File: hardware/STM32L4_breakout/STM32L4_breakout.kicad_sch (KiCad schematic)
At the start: 66 parts, among them J1 12V IN, J10 GPIO, J12 USART1, J13 USART3, J15 3.3V, J16 5V, J17 12V, J2 SWD, J3 Conn_01x08, J4 Conn_01x06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

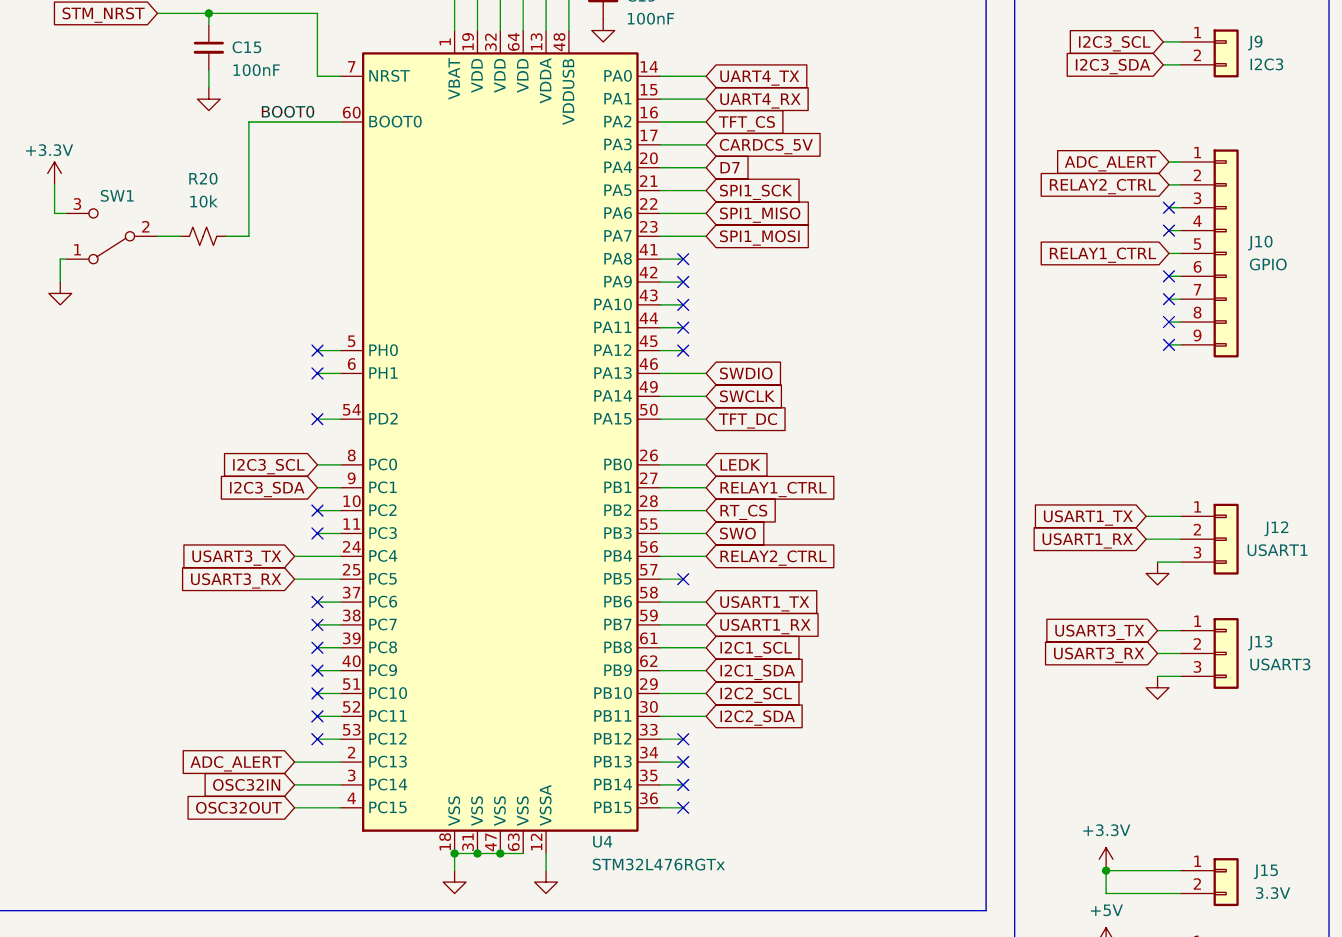
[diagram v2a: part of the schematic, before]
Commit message: moved GPIO signals on schematic
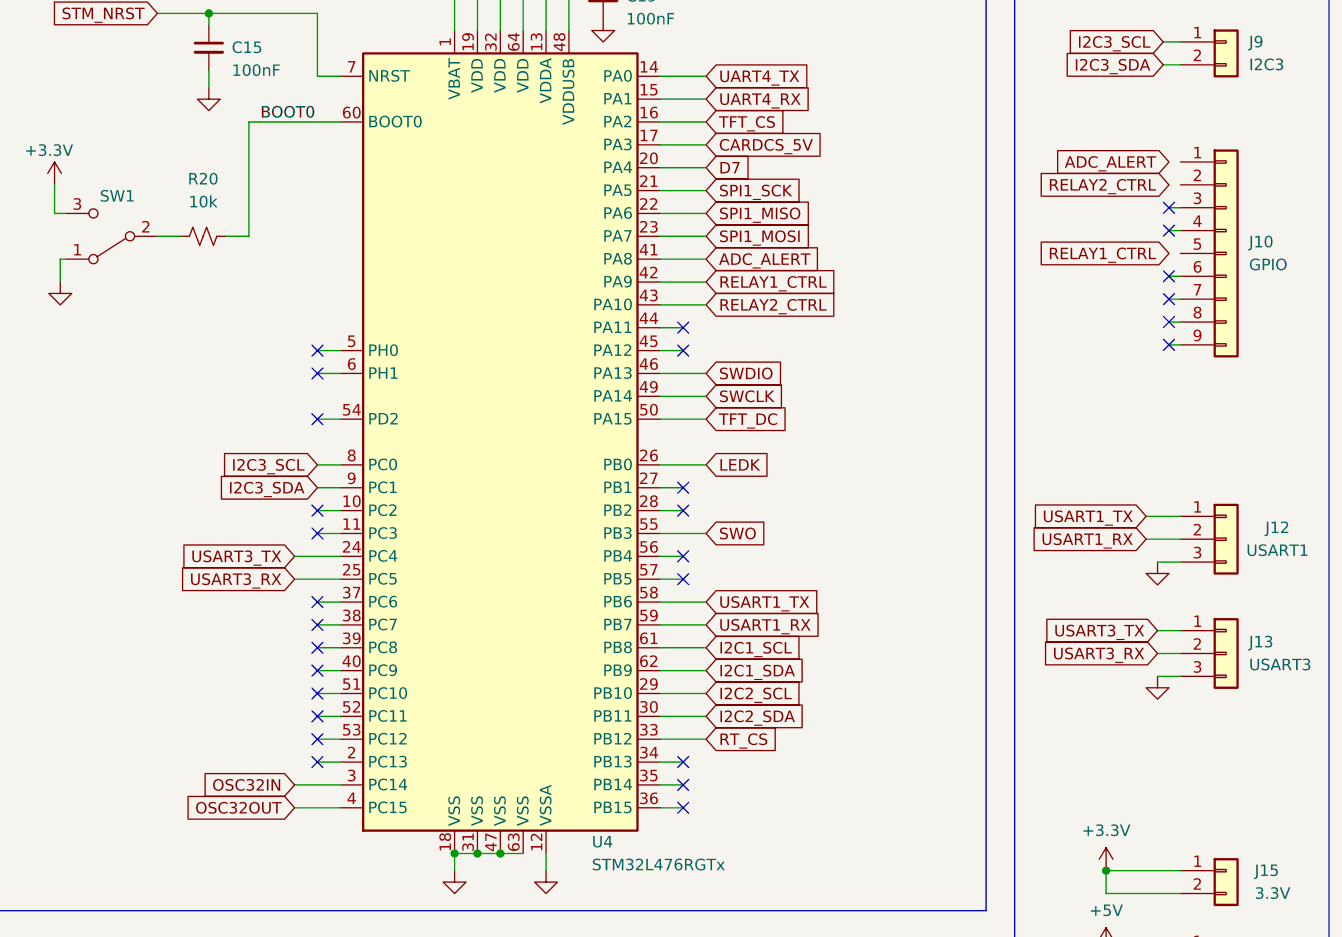
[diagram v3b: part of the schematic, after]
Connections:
- net ADC_ALERT: now also U4.41 (PA8); no longer J10.1 (Pin_1), U4.2 (PC13)
- net RELAY1_CTRL: now also U4.42 (PA9); no longer J10.5 (Pin_5), U4.27 (PB1)
- net RELAY2_CTRL: now also U4.43 (PA10); no longer J10.2 (Pin_2), U4.56 (PB4)
- net RT_CS: now also U4.33 (PB12); no longer U4.28 (PB2)
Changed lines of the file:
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@@
   (junction (at 159.385 36.83) (diameter 0) (color 0 0 0 0)
   )
-  (no_connect (at 209.55 125.73))
+  (no_connect (at 209.55 97.79))
   (no_connect (at 24.13 183.515))
   (no_connect (at 168.91 82.55))
@@
   (no_connect (at 24.13 178.435))
   (no_connect (at 62.865 180.975))
-  (no_connect (at 209.55 72.39))
   (no_connect (at 168.91 100.33))
-  (no_connect (at 209.55 77.47))
   (no_connect (at 168.91 120.65))
-  (no_connect (at 209.55 74.93))
   (no_connect (at 263.525 81.915))
   (no_connect (at 263.525 66.675))
@@
   (no_connect (at 209.55 130.81))
   (no_connect (at 168.91 123.19))
+  (no_connect (at 209.55 105.41))
   (no_connect (at 263.525 76.835))
+  (no_connect (at 209.55 100.33))
+  (no_connect (at 168.91 128.27))
   (no_connect (at 168.91 125.73))
   (no_connect (at 24.13 180.975))
@@
     (stroke (width 0) (type default) (color 0 0 0 0))
   )
+  (wire (pts (xy 207.01 72.39) (xy 212.09 72.39))
+    (stroke (width 0) (type default) (color 0 0 0 0))
+  )
+  (wire (pts (xy 209.55 105.41) (xy 207.01 105.41))
+    (stroke (width 0) (type default) (color 0 0 0 0))
+  )
   (polyline (pts (xy 174.625 193.675) (xy 174.625 150.495))
     (stroke (width 0) (type default) (color 0 0 0 0))
@@
     (stroke (width 0) (type default) (color 0 0 0 0))
   )
-  (wire (pts (xy 263.525 61.595) (xy 264.795 61.595))
-    (stroke (width 0) (type default) (color 0 0 0 0))
-  )
   (polyline (pts (xy 76.835 82.55) (xy 76.2 82.55))
     (stroke (width 0) (type default) (color 0 0 0 0))
@@
     (stroke (width 0) (type default) (color 0 0 0 0))
   )
+  (wire (pts (xy 207.01 77.47) (xy 212.09 77.47))
+    (stroke (width 0) (type default) (color 0 0 0 0))
+  )
   (polyline (pts (xy 13.97 76.2) (xy 124.46 76.2))
     (stroke (width 0) (type default) (color 0 0 0 0))
@@
     (stroke (width 0) (type default) (color 0 0 0 0))
   )
-  (wire (pts (xy 207.01 125.73) (xy 209.55 125.73))
-    (stroke (width 0) (type default) (color 0 0 0 0))
-  )
   (wire (pts (xy 149.86 180.34) (xy 131.445 180.34))
     (stroke (width 0) (type default) (color 0 0 0 0))
@@
     (stroke (width 0) (type default) (color 0 0 0 0))
   )
+  (wire (pts (xy 209.55 97.79) (xy 207.01 97.79))
+    (stroke (width 0) (type default) (color 0 0 0 0))
+  )
   (wire (pts (xy 35.56 26.035) (xy 35.56 30.48))
     (stroke (width 0) (type default) (color 0 0 0 0))
@@
     (stroke (width 0) (type default) (color 0 0 0 0))
   )
-  (wire (pts (xy 263.525 64.135) (xy 264.795 64.135))
-    (stroke (width 0) (type default) (color 0 0 0 0))
-  )
   (wire (pts (xy 151.13 45.085) (xy 156.845 45.085))
     (stroke (width 0) (type default) (color 0 0 0 0))
@@
     (stroke (width 0) (type default) (color 0 0 0 0))
   )
-  (wire (pts (xy 166.37 128.27) (xy 171.45 128.27))
-    (stroke (width 0) (type default) (color 0 0 0 0))
-  )
   (wire (pts (xy 262.89 48.26) (xy 264.795 48.26))
     (stroke (width 0) (type default) (color 0 0 0 0))
@@
     (stroke (width 0) (type default) (color 0 0 0 0))
   )
-  (wire (pts (xy 207.01 74.93) (xy 209.55 74.93))
-    (stroke (width 0) (type default) (color 0 0 0 0))
-  )
   (wire (pts (xy 231.14 29.21) (xy 239.395 29.21))
     (stroke (width 0) (type default) (color 0 0 0 0))
@@
     (stroke (width 0) (type default) (color 0 0 0 0))
   )
+  (wire (pts (xy 207.01 125.73) (xy 212.09 125.73))
+    (stroke (width 0) (type default) (color 0 0 0 0))
+  )
   (wire (pts (xy 213.36 27.94) (xy 213.36 29.21))
     (stroke (width 0) (type default) (color 0 0 0 0))
@@
     (stroke (width 0) (type default) (color 0 0 0 0))
   )
-  (wire (pts (xy 207.01 72.39) (xy 209.55 72.39))
-    (stroke (width 0) (type default) (color 0 0 0 0))
-  )
   (wire (pts (xy 62.865 140.335) (xy 65.405 140.335))
     (stroke (width 0) (type default) (color 0 0 0 0))
@@
     (stroke (width 0) (type default) (color 0 0 0 0))
   )
-  (wire (pts (xy 207.01 100.33) (xy 212.09 100.33))
-    (stroke (width 0) (type default) (color 0 0 0 0))
-  )
   (wire (pts (xy 97.79 149.86) (xy 97.79 142.875))
     (stroke (width 0) (type default) (color 0 0 0 0))
@@
     (stroke (width 0) (type default) (color 0 0 0 0))
   )
+  (wire (pts (xy 168.91 128.27) (xy 171.45 128.27))
+    (stroke (width 0) (type default) (color 0 0 0 0))
+  )
   (wire (pts (xy 260.985 100.965) (xy 264.795 100.965))
     (stroke (width 0) (type default) (color 0 0 0 0))
@@
     (stroke (width 0) (type default) (color 0 0 0 0))
   )
+  (wire (pts (xy 209.55 100.33) (xy 207.01 100.33))
+    (stroke (width 0) (type default) (color 0 0 0 0))
+  )
   (wire (pts (xy 166.37 107.95) (xy 171.45 107.95))
     (stroke (width 0) (type default) (color 0 0 0 0))
@@
     (stroke (width 0) (type default) (color 0 0 0 0))
   )
-  (wire (pts (xy 207.01 97.79) (xy 212.09 97.79))
-    (stroke (width 0) (type default) (color 0 0 0 0))
-  )
   (wire (pts (xy 207.01 130.81) (xy 209.55 130.81))
     (stroke (width 0) (type default) (color 0 0 0 0))
@@
     (stroke (width 0) (type default) (color 0 0 0 0))
   )
-  (wire (pts (xy 263.525 71.755) (xy 264.795 71.755))
-    (stroke (width 0) (type default) (color 0 0 0 0))
-  )
   (wire (pts (xy 29.845 158.115) (xy 29.845 161.925))
     (stroke (width 0) (type default) (color 0 0 0 0))
@@
     (stroke (width 0) (type default) (color 0 0 0 0))
   )
-  (wire (pts (xy 207.01 77.47) (xy 209.55 77.47))
-    (stroke (width 0) (type default) (color 0 0 0 0))
-  )
   (wire (pts (xy 207.01 123.19) (xy 212.09 123.19))
     (stroke (width 0) (type default) (color 0 0 0 0))
@@
     (stroke (width 0) (type default) (color 0 0 0 0))
   )
+  (wire (pts (xy 207.01 74.93) (xy 212.09 74.93))
+    (stroke (width 0) (type default) (color 0 0 0 0))
+  )
   (wire (pts (xy 92.71 38.1) (xy 92.71 38.735))
     (stroke (width 0) (type default) (color 0 0 0 0))
   )
   (wire (pts (xy 262.255 118.745) (xy 264.795 118.745))
-    (stroke (width 0) (type default) (color 0 0 0 0))
-  )
-  (wire (pts (xy 207.01 105.41) (xy 212.09 105.41))
     (stroke (width 0) (type default) (color 0 0 0 0))
   )
@@
     )
   )
-  (global_label "ADC_ALERT" (shape input) (at 166.37 128.27 180) (fields_autoplaced)
-    (effects (font (size 1.27 1.27)) (justify right))
-    (property "Intersheet References" "${INTERSHEET_REFS}" (id 0) (at 153.8574 128.1906 0)
-      (effects (font (size 1.27 1.27)) (justify right) hide)
+  (global_label "ADC_ALERT" (shape input) (at 212.09 72.39 0) (fields_autoplaced)
+    (effects (font (size 1.27 1.27)) (justify left))
+    (property "Intersheet References" "${INTERSHEET_REFS}" (id 0) (at 224.6026 72.3106 0)
+      (effects (font (size 1.27 1.27)) (justify left) hide)
     )
   )
@@
     )
   )
-  (global_label "RT_CS" (shape input) (at 212.09 100.33 0) (fields_autoplaced)
-    (effects (font (size 1.27 1.27)) (justify left))
-    (property "Intersheet References" "${INTERSHEET_REFS}" (id 0) (at 220.1879 100.2506 0)
+  (global_label "RT_CS" (shape input) (at 212.09 125.73 0) (fields_autoplaced)
+    (effects (font (size 1.27 1.27)) (justify left))
+    (property "Intersheet References" "${INTERSHEET_REFS}" (id 0) (at 220.1879 125.6506 0)
       (effects (font (size 1.27 1.27)) (justify left) hide)
     )
@@
     )
   )
-  (global_label "RELAY1_CTRL" (shape input) (at 212.09 97.79 0) (fields_autoplaced)
-    (effects (font (size 1.27 1.27)) (justify left))
-    (property "Intersheet References" "${INTERSHEET_REFS}" (id 0) (at 226.8402 97.7106 0)
+  (global_label "RELAY1_CTRL" (shape input) (at 212.09 74.93 0) (fields_autoplaced)
+    (effects (font (size 1.27 1.27)) (justify left))
+    (property "Intersheet References" "${INTERSHEET_REFS}" (id 0) (at 226.8402 74.8506 0)
       (effects (font (size 1.27 1.27)) (justify left) hide)
     )
@@
     )
   )
-  (global_label "RELAY2_CTRL" (shape input) (at 212.09 105.41 0) (fields_autoplaced)
-    (effects (font (size 1.27 1.27)) (justify left))
-    (property "Intersheet References" "${INTERSHEET_REFS}" (id 0) (at 226.8402 105.3306 0)
-      (effects (font (size 1.27 1.27)) (justify left) hide)
-    )
+  (global_label "RELAY2_CTRL" (shape input) (at 212.09 77.47 0) (fields_autoplaced)
+    (effects (font (size 1.27 1.27)) (justify left))
+    (property "Intersheet References" "${INTERSHEET_REFS}" (id 0) (at 226.8402 77.3906 0)
+      (effects (font (size 1.27 1.27)) (justify left) hide)
+    )

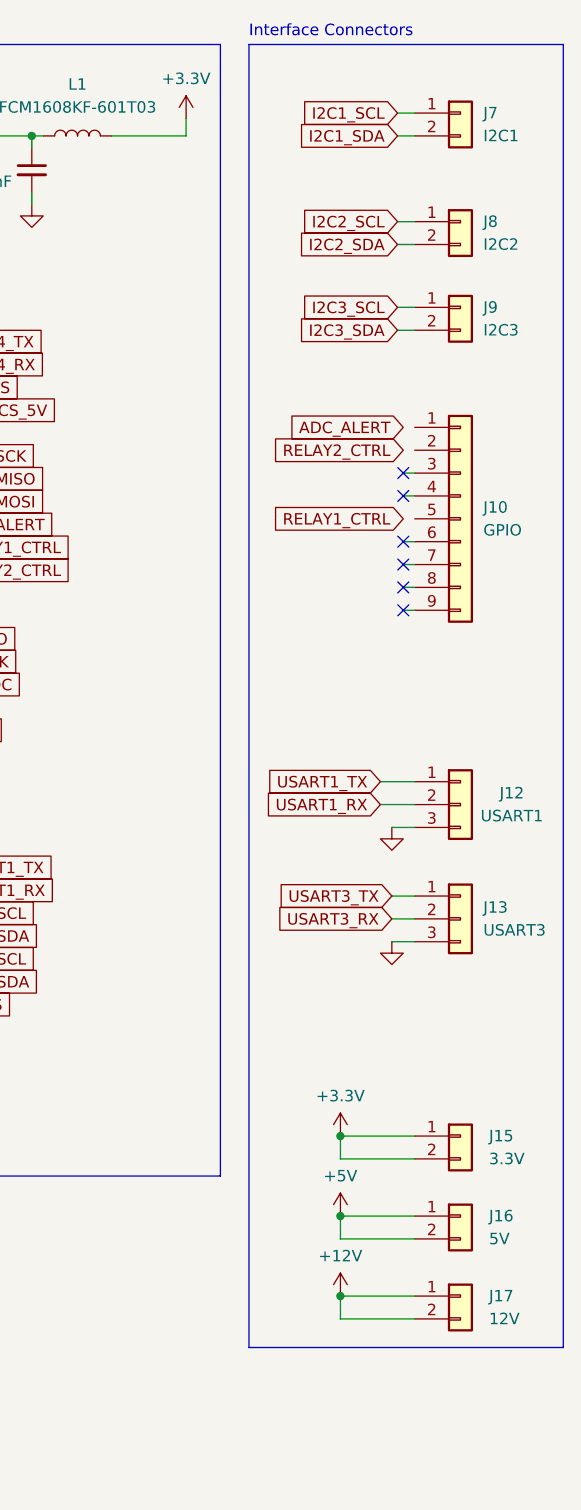
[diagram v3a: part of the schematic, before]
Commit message: signal routing complete
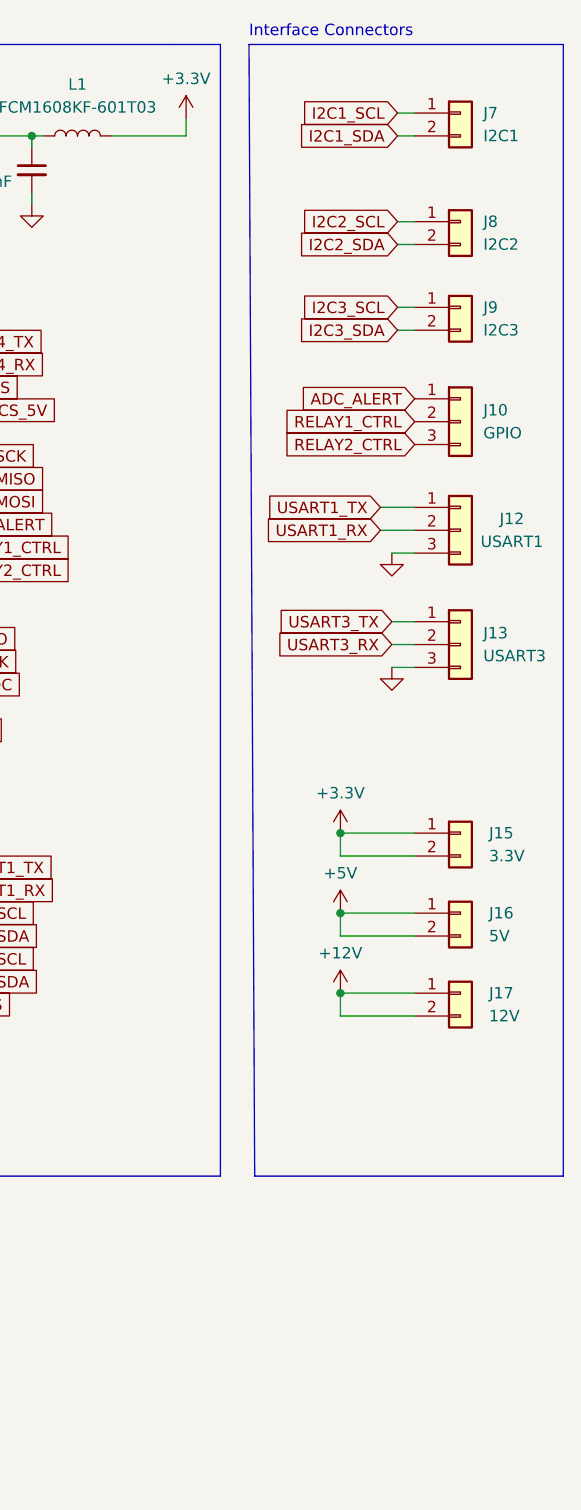
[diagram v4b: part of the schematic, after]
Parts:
- J10: footprint Connector_PinHeader_2.54mm:PinHeader_1x09_P2.54mm_Vertical -> Connector_PinSocket_2.54mm:PinSocket_1x03_P2.54mm_Vertical; symbol Connector_Generic:Conn_01x09 -> Connector_Generic:Conn_01x03
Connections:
- net ADC_ALERT: now also J10.1 (Pin_1)
- net RELAY1_CTRL: now also J10.2 (Pin_2)
- net RELAY2_CTRL: now also J10.3 (Pin_3)
- no-connect marks 38 -> 32
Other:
- moved on the sheet: J12, J13, J15, J16, J17
